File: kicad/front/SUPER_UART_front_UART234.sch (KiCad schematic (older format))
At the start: 48 parts, among them CON2 UART B, CON3 UART C, CON4 UART D, U3 SN74LVC2T45DCTT, U4 SN74LVC2T45DCTT, U5 SN74LVC2T45DCTT, U6 SN74LVC2T45DCTT, U7 SN74LVC2T45DCTT, U8 SN74LVC2T45DCTT, U9 74HC595D

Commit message: Working on schematic
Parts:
- removed C13, C16: 100n, 0603_N, symbol C
- removed CON4: UART D, pnConnector:NIGINI_NCDW-06, symbol PIN-1x6
- removed D21: DTR, pnSemiconductor:LED0603_R, symbol diode_LED
- removed D22: RXD, pnSemiconductor:LED0603_R, symbol diode_LED
- removed D23: TXD, pnSemiconductor:LED0603_R, symbol diode_LED
- removed D24: CTS, pnSemiconductor:LED0603_R, symbol diode_LED
- removed D7, D8: PESD5V2S2UT, SOT23-3_N, symbol PESD5V2S2UT
- removed RN3, RN4: R, pnRLC:4x0603_N, symbol R_network_4
- removed RN6, RN7: R, 4x0603_N, symbol R_Network_4
- removed U3, U4, U5, U7, U8: SN74LVC2T45DCTT, niceSemiconductors:TI_SSOP-8_N, symbol SN74LVC2T45DCTT
- added Q2, Q3: PDTA143ZT, niceSemiconductors:SOT23-3_N, symbol PDTA143ZT
- added R11, R19: R, 0603_R_N, symbol R_V
- added R12, R20, R21, R22: R, 0603_R_N, symbol R
- added RN7: R, pnRLC:4x0603_N, symbol R_network_4
- added T1, T4: DMG1012UW-7, niceSemiconductors:SC70-3_N, symbol N-MOS_small
- added TP10, TP11, TP12: Testpoint, pnConnector:TP_1mm, symbol Testpoint
- added U2, U3: 74LVC1T45GW, SC70-6_N, symbol 74LVC1T45GW
- added U20: 74LVC8T245PW, TI_TSSOP-24_N, symbol 74LVC8T245PW
- U6: value SN74LVC2T45DCTT -> 74LVC2T45DCU; footprint niceSemiconductors:TI_SSOP-8_N -> niceSemiconductors:TI_VSSOP-8_N; symbol SN74LVC2T45DCTT -> 74LVC2T45DCU
- U9: footprint SOIC-16_N -> niceSemiconductors:TSSOP-16_N; symbol 74HC595D -> 74HC595PW
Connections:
- net labels added: CTS_A, CTS_A_VDDB, CTS_C_VDDB, DTR_A, DTR_A_VDDB, DTR_C_VDDB, EECLK, EECS, EEDATA, I2C_PU_EN_A, I2C_PU_EN_A_VCCB, PWREN, RXD_A, RXD_A_VDDB, RXD_C_VDDB, SPI_EN_A, TXD_A, TXD_A_VDDB, TXD_C_VDDB, VDDB, ~CTS_A_OC, ~RXD_A_OC
- net labels removed: CTS_B, CTS_D, DTR_B, DTR_D, FTDI_EECLK, FTDI_EECS, FTDI_EEDATA, FTDI_PWREN, FT_CTS_B, FT_CTS_C, FT_CTS_D, FT_DTR_B, FT_DTR_C, FT_DTR_D, FT_RXD_B, FT_RXD_C, FT_RXD_D, FT_TXD_B, FT_TXD_C, FT_TXD_D, RXD_B, RXD_D, TXD_B, TXD_D, VDD
- wire segments 217 -> 182
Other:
- moved on the sheet: C1, C10, C11, C12, C18, C2, C3, C8, C9, CON2, CON3, D13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

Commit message: Working on schematic
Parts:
- removed T1, T4: DMG1012UW-7, niceSemiconductors:SC70-3_N, symbol N-MOS_small
- removed TP10, TP11, TP12: Testpoint, pnConnector:TP_1mm, symbol Testpoint
- added C42, C48: 100n, 0603_N, symbol C
- added C43: 10n, 0603_N, symbol C
- added C44: 10u, niceRLC:0805_N, symbol C
- added C47: 1u, niceRLC:0603_N, symbol C
- added Q10, Q8: 2N7002PS, niceSemiconductors:SC70-6_N, symbol 2N7002PS
- added Q11: N-MOS_small, SOT23-3_N, symbol N-MOS_small
- added R34, R35, R37, R38, R41, R45: 10k, 0603_R_N, symbol R_V
- added R40: 4k7, 0603_R_N, symbol R_V
- added R42: 1k8, 0603_R_N, symbol R_V
- added R43: 3k9, 0603_R_N, symbol R_V
- added R44: 6k8, 0603_R_N, symbol R_V
- added R46: 5k6, 0603_R_N, symbol R
- added R47: 47k, 0603_R_N, symbol R
- added U16: LP2951CD, SOIC-8_N, symbol LP2951CD
- renumbered C18 to C33, C14 to C34, C2 to C35, C1 to C36, C3 to C37, C12 to C38, C11 to C39, C9 to C40, C15 to C41, C10 to C45, C8 to C46, CON2 to CON7, CON3 to CON8, D3 to D10, D4 to D11, D5 to D12, D6 to D13, D13 to LED35, D16 to LED36, D14 to LED37, D15 to LED38, D17 to LED39, D20 to LED40, D18 to LED41, D19 to LED42, Q2 to Q7, Q3 to Q9, R5 to R29, R21 to R30, R22 to R31, R11 to R32, R12 to R33, R19 to R36, R20 to R39, RN5 to RN8, RN2 to RN9, U9 to U11, U20 to U12, U6 to U13, U2 to U14, U3 to U15
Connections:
- net labels added: +5V, CTS_A_VDD2, CTS_C_VDD2, DTR_A_VDD2, DTR_C_VDD2, RXD_A_VDD2, RXD_C_VDD2, TXD_A_VDD2, TXD_C_VDD2, VDD2, VDD2_SEL1, VDD2_SEL2, VDD2_SEL3, ~PWREN, ~VDD2_EN, ~VDD2_ERR
- net labels removed: CTS_A_VDDB, CTS_C_VDDB, DTR_A_VDDB, DTR_C_VDDB, PWREN, RXD_A_VDDB, RXD_C_VDDB, TXD_A_VDDB, TXD_C_VDDB, VDDB
- wire segments 182 -> 229
- no-connect marks 1 -> 6
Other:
- moved on the sheet: C37, C38, C39, C40, C45, C46, Q7, Q9, R30, R31, R32, R33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

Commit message: Working on schematic
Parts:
- CON7: value UART B -> PORT A
- CON8: value UART C -> PORT C
- LED35, LED36, LED37, LED38, LED39, LED40, LED41, LED42: footprint pnSemiconductor:LED0603_R -> pnSemiconductor:0805D

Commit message: PCB placement
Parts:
- removed Q8: 2N7002PS, niceSemiconductors:SC70-6_N, symbol 2N7002PS
- added Q13, Q14: N-MOS_small, SOT23-3_N, symbol N-MOS_small
- RN7, RN9: footprint pnRLC:4x0603_N -> niceRLC:4x0603_N
- RN8: footprint 4x0603_N -> niceRLC:4x0603_N
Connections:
- net CTS_A_VDD2: now also Q13.3 (D)
- net DTR_A_VDD2: now also RN7.3; no longer RN7.2
- net DTR_C_VDD2: now also RN7.1; no longer RN7.4
- net GND: now also Q13.2 (S), Q14.2 (S)
- net RXD_A_VDD2: now also Q14.3 (D)
- net TXD_A_VDD2: now also RN7.4; no longer RN7.1
- net TXD_C_VDD2: now also RN7.2; no longer RN7.3
- net VDD2_SEL1: now also Q11.1 (G); no longer Q10.1 (G)
- net VDD2_SEL3: now also Q10.1 (G); no longer Q11.1 (G)
- net ~CTS_A_OC: now also Q13.1 (G)
- net ~RXD_A_OC: now also Q14.1 (G)
- net at U12.18 (B4): now also RN7.8; no longer RN7.5
- net at U12.19 (B3): now also RN7.7; no longer RN7.6
- net at U12.20 (B2): now also RN7.6; no longer RN7.7
- net at U12.21 (B1): now also RN7.5; no longer RN7.8
- net at C48.1, R42.1, R47.2: now also Q11.3 (D); no longer Q10.6 (D)
- net at R44.1: now also Q10.6 (D); no longer Q11.3 (D)
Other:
- moved on the sheet: Q10A, Q11

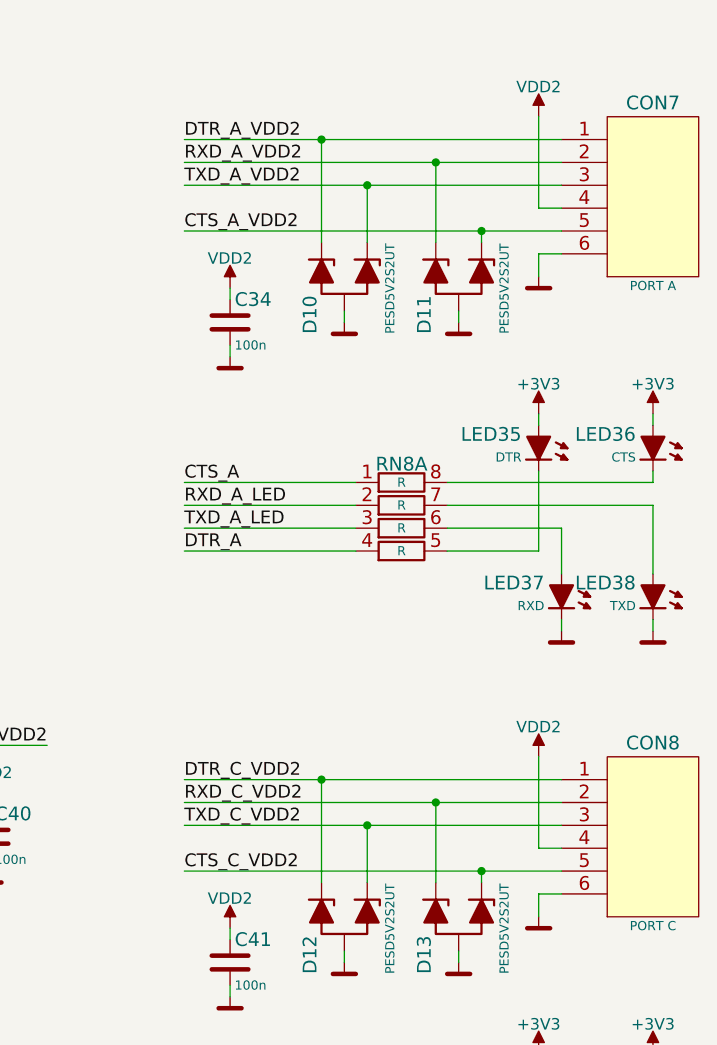
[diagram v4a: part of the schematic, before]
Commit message: Routing before moving to 4 layers
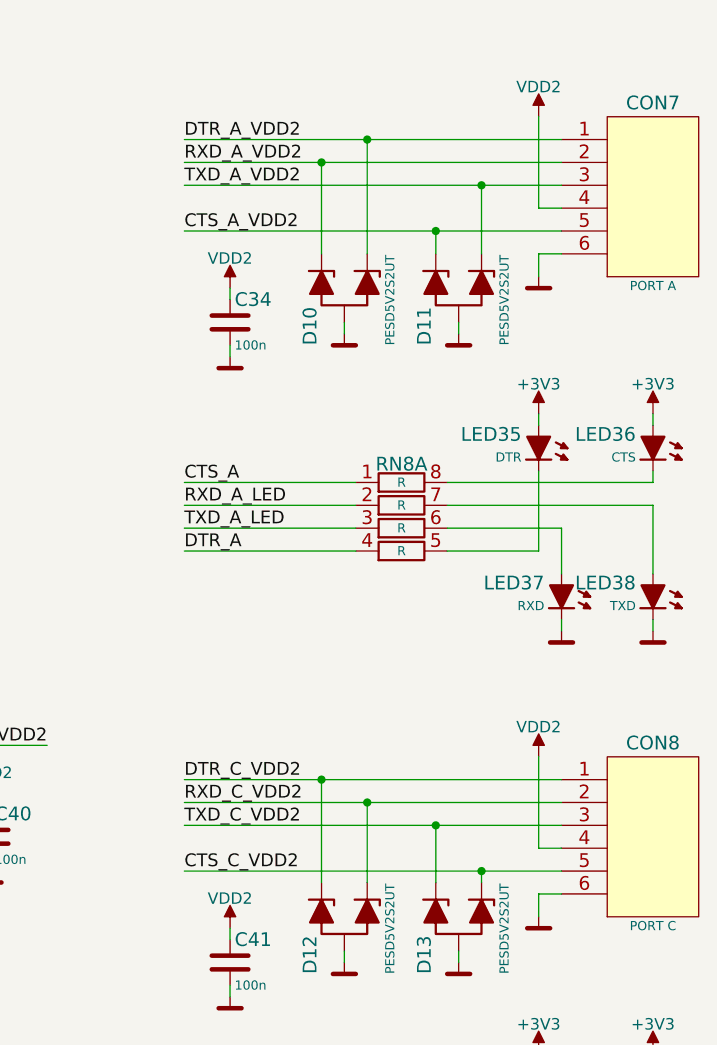
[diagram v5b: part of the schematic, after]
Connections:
- net CTS_A_VDD2: now also D11.1 (C1); no longer D11.2 (C2)
- net DTR_A_VDD2: now also D10.2 (C2); no longer D10.1 (C1)
- net RXD_A_VDD2: now also D10.1 (C1); no longer D11.1 (C1)
- net RXD_C_VDD2: now also D12.2 (C2); no longer D13.1 (C1)
- net TXD_A_VDD2: now also D11.2 (C2); no longer D10.2 (C2)
- net TXD_C_VDD2: now also D13.1 (C1); no longer D12.2 (C2)
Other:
- moved on the sheet: D10, D11

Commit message: Front board routed
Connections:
- net DTR_A: now also U12.3 (A1); no longer U12.4 (A2)
- net DTR_A_VDD2: now also RN7.4; no longer RN7.3
- net TXD_A: now also U12.4 (A2); no longer U12.3 (A1)
- net TXD_A_VDD2: now also RN7.3; no longer RN7.4

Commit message: Add missing files
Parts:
- Q10: value 2N7002PS -> N.C.
- Q11: value N-MOS_small -> N.C.
- R30, R31, R33, R39, RN7: value R -> 100R
- R32: value R -> 4k7; Fieldname (none) -> Value
- R36: value R -> 4k7
- R40: value 4k7 -> 100k
- R42: value 1k8 -> 47k
- R43: value 3k9 -> N.C.
- R44: value 6k8 -> N.C.
- R45: value 10k -> 47k
- RN8, RN9: value R -> 1k
- U11: value 74HC595D -> 74HC595P; Fieldname (none) -> Value
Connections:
- net I2C_PU_EN_A_VCCB: no longer Q7.1 (B), U12.17 (B5)
- net I2C_PU_EN_A renamed ~I2C_PU_EN_A
- new net ~I2C_PU_EN_A_VCCB: Q7.1 (B), U12.17 (B5)
